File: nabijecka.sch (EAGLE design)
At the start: 69 parts, among them T1 BD244C, T2 BD244C, T3 BC556, T4 BC556, T5 BD244C, T6 BC556, U1 TINY45-20-DIP, X1 04-JST-B4B-XH-A

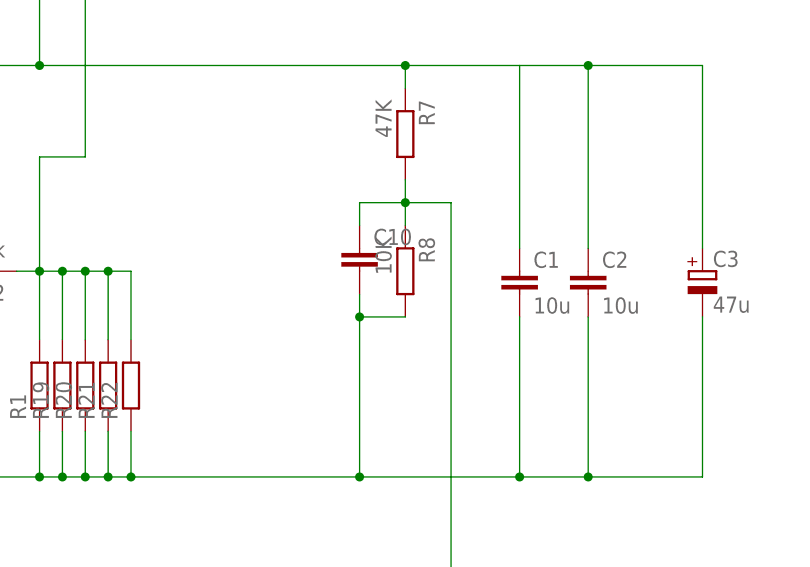
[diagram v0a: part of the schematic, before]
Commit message: Add schema in PDF. Rename files.
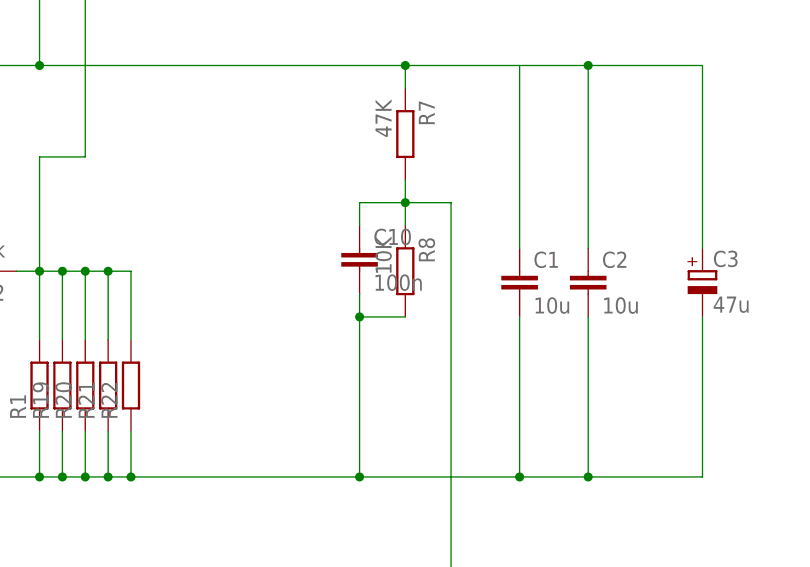
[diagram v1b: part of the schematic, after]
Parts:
- C10: value (none) -> 100n
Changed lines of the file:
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@@
 <part name="R7" library="resistor" deviceset="R-EU_" device="R1206" value="47K"/>
 <part name="R8" library="resistor" deviceset="R-EU_" device="R1206" value="10K"/>
-<part name="C10" library="resistor" deviceset="C-EU" device="C1206"/>
+<part name="C10" library="resistor" deviceset="C-EU" device="C1206" value="100n"/>
 <part name="T1" library="transistor" deviceset="*-PNP-" device="TO220" value="BD244C"/>
 <part name="D3" library="diode" deviceset="DIODE-" device="SOD80C" value="1N4148"/>
